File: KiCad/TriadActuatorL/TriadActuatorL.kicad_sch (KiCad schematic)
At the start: 54 parts, among them J1 USB_C_Receptacle_USB2.0_16P, J2 Motor Terminal, J3 PWR Terminal, J4 Conn_01x02_Pin, J5 Conn_01x02_Pin, Q1 AO3401A, U1 MT6701CT, U2 STM32G431C6Ux, U3 DRV8316CRRGFR, U4 CA-IF1042LVS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

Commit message: updated can model
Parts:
- removed SPI_Conn1: Conn_01x05_Pin, Connector_JST:JST_PH_S5B-PH-K_1x05_P2.00mm_Horizontal, symbol Connector:Conn_01x05_Pin
- removed qwicc1: Conn_01x04_Pin, Connector_JST:JST_PH_S4B-PH-K_1x04_P2.00mm_Horizontal, symbol Connector:Conn_01x04_Pin
- added C27: 0.1uF, symbol Device:C
- added J6: Conn_01x05_Pin, symbol Connector:Conn_01x05_Pin
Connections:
- net 3V3: now also U4.5 (VIO), C27.2
- net 5V: now also J6.1 (Pin_1)
- net GND: now also U4.2 (GND), U4.8 (STB), C27.1, J6.2 (Pin_2)
- net LED_PC6: now also U2.29 (PC6)
- net SPI2_MISO: now also J6.5 (Pin_5)
- net SPI2_MOSI: now also J6.4 (Pin_4)
- net SPI2_SCK: now also J6.3 (Pin_3)
- net I2C_SCL: no longer names the net of U2.36 (PA13)
- net I2C_SDA: no longer names the net of U2.37 (PA14)
- no-connect marks 30 -> 31
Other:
- moved on the sheet: C1, C10, C11, C12, C13, C14, C15, C16, C17, C18, C19, C2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

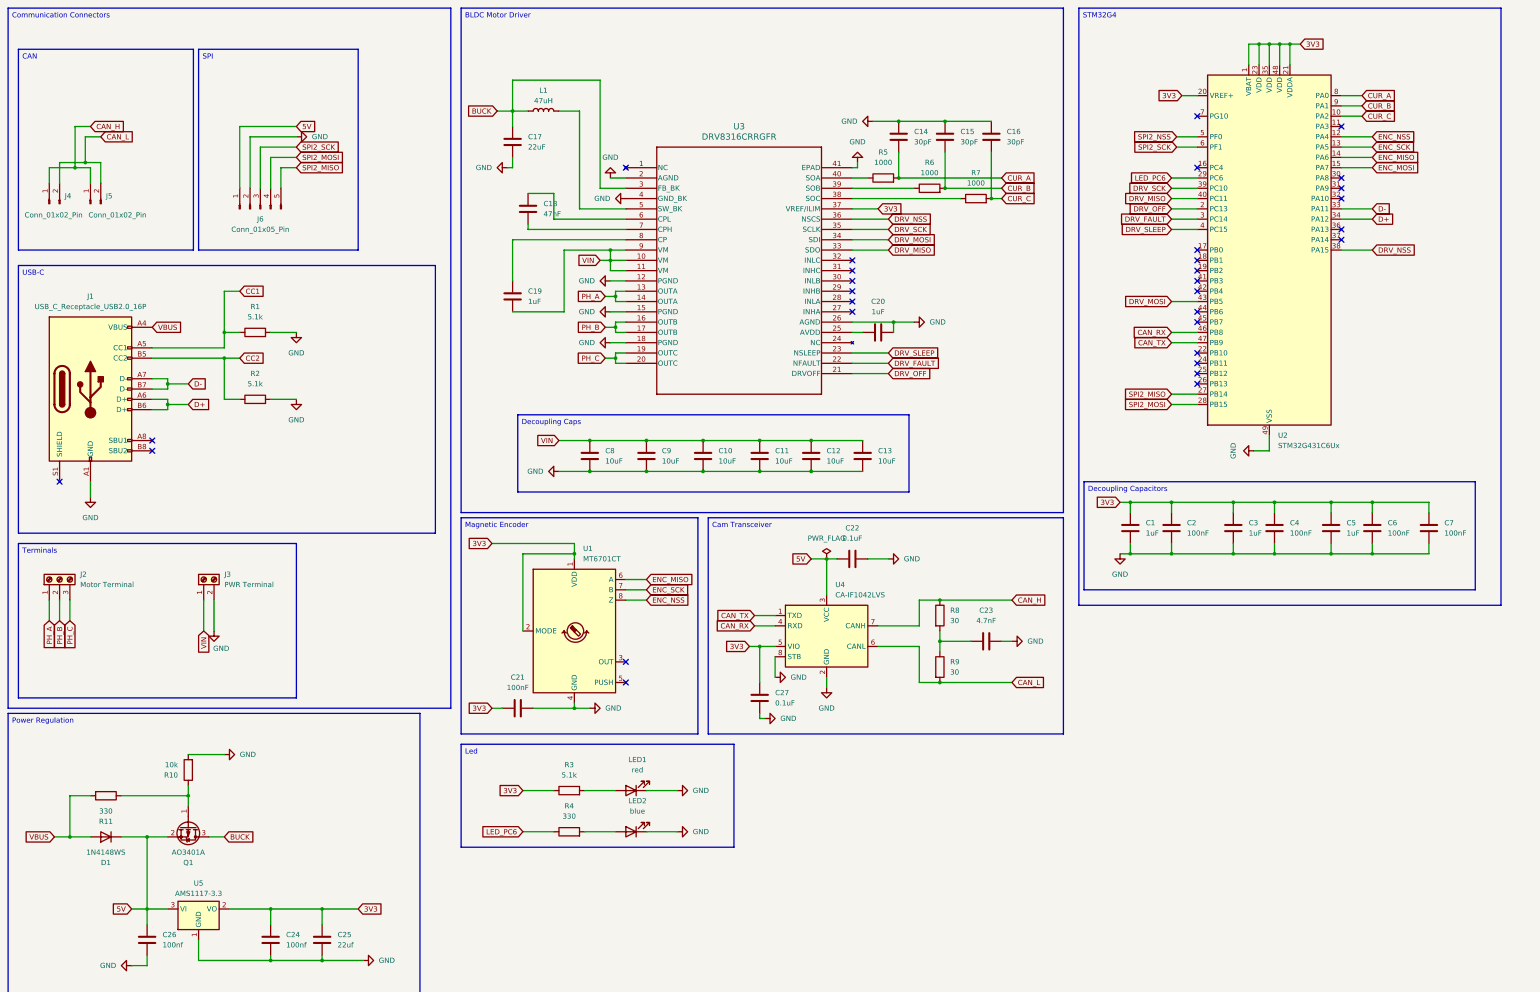
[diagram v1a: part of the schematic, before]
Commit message: Added Getting started doc for stm32G4
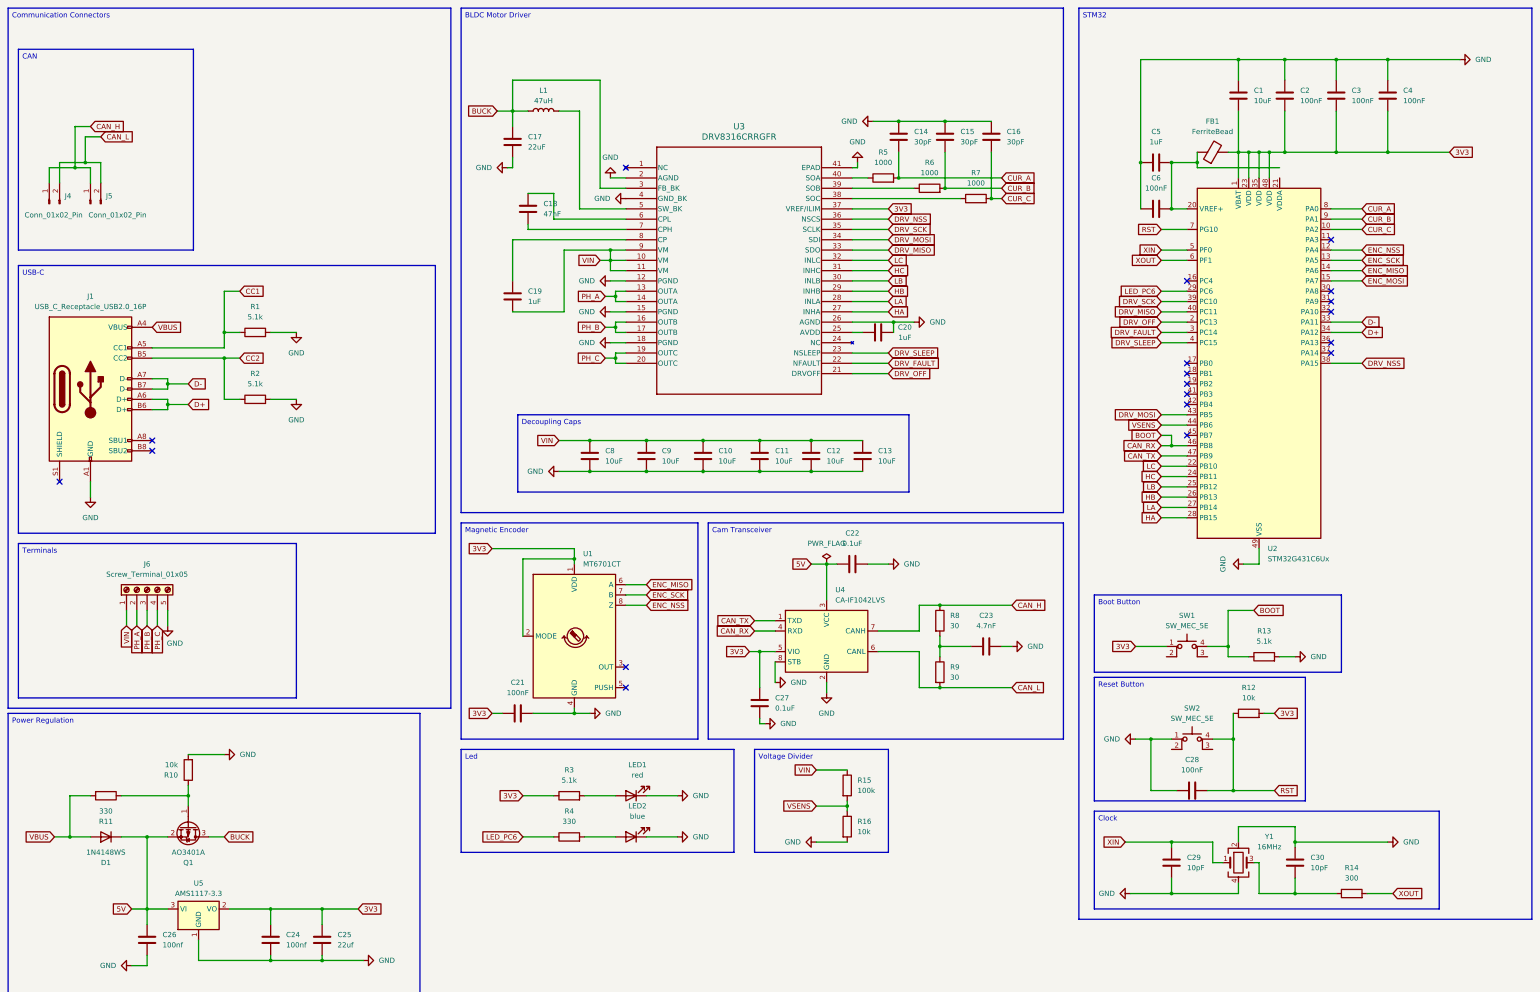
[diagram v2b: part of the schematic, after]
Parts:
- removed C7: 100nF, Capacitor_SMD:C_0402_1005Metric, symbol Device:C
- removed J2: Motor Terminal, TerminalBlock_WAGO:TerminalBlock_WAGO_233-502_2x02_P2.54mm, symbol Connector:Screw_Terminal_01x03
- removed J3: PWR Terminal, TerminalBlock_WAGO:TerminalBlock_WAGO_233-503_2x03_P2.54mm, symbol Connector:Screw_Terminal_01x02
- removed J6: Conn_01x05_Pin, symbol Connector:Conn_01x05_Pin
- added C28: 100nF, symbol Device:C
- added C29, C30: 10pF, symbol Device:C
- added FB1: FerriteBead, symbol Device:FerriteBead
- added J6: Screw_Terminal_01x05, symbol Connector:Screw_Terminal_01x05
- added R12, R16: 10k, symbol Device:R
- added R13: 5.1k, symbol Device:R
- added R14: 300, symbol Device:R
- added R15: 100k, symbol Device:R
- added SW1, SW2: SW_MEC_5E, Button_Switch_SMD:SW_MEC_5GSH9, symbol Switch:SW_MEC_5E
- added Y1: 16MHz, Crystal:Crystal_SMD_0603-4Pin_6.0x3.5mm, symbol Device:Crystal_GND24
- C1: value 1uF -> 10uF; footprint Capacitor_SMD:C_0402_1005Metric -> (none)
- C2, C4, C5, C6: footprint Capacitor_SMD:C_0402_1005Metric -> (none)
- C3: value 1uF -> 100nF; footprint Capacitor_SMD:C_0402_1005Metric -> (none)
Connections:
- net SPI2_MISO is gone; now on net LA: U2.27 (PB14)
- net SPI2_MOSI is gone; now on net HA: U2.28 (PB15)
- net 3V3: now also FB1.2, R12.2, SW1.1; no longer C5.1, C6.1, U2.20 (VREF+), U2.21 (VDDA)
- net GND: now also C5.1, C6.1, C28.1, C29.1, C30.1, J6.5 (Pin_5), R13.2, R16.2, SW2.1, Y1.2, Y1.4; no longer C5.2, C6.2
- net PH_A: now also J6.2 (Pin_2)
- net PH_B: now also J6.3 (Pin_3)
- net PH_C: now also J6.4 (Pin_4)
- net VIN: now also J6.1 (Pin_1), R15.1
- net HA: now reaches U3.27 (INHA)
- net LA: now reaches U3.28 (INLA)
- net HB: now reaches U3.29 (INHB)
- net HB: now also U2.26 (PB13)
- net LB: now reaches U3.30 (INLB)
- net LB: now also U2.25 (PB12)
- net HC: now reaches U3.31 (INHC)
- net HC: now also U2.24 (PB11)
- net LC: now reaches U3.32 (INLC)
- net LC: now also U2.22 (PB10)
- net VSENS: now reaches U2.44 (PB6)
- net VSENS: now also R15.2, R16.1
- net RST: now reaches U2.7 (PG10)
- net RST: now also C28.2, R12.1, SW2.4 (A)
- net CAN_RX renamed BOOT
- net BOOT: now also R13.1, SW1.4 (A)
- net SPI2_NSS renamed XIN
- net XIN: now also C29.2, Y1.1
- net SPI2_SCK renamed XOUT
- net XOUT: now also R14.2
- new net: C5.2, C6.2, FB1.1, U2.20 (VREF+)
- new net: C30.2, R14.1, Y1.3
- no-connect marks 31 -> 19
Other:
- moved on the sheet: C21, C22, C23, C27, LED1, LED2, R3, R4, R8, R9, U1, U2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
